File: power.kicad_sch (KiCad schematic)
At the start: 4 parts, among them J1 USB_C_Receptacle_USB2.0_14P, U3 BQ51051BRHL

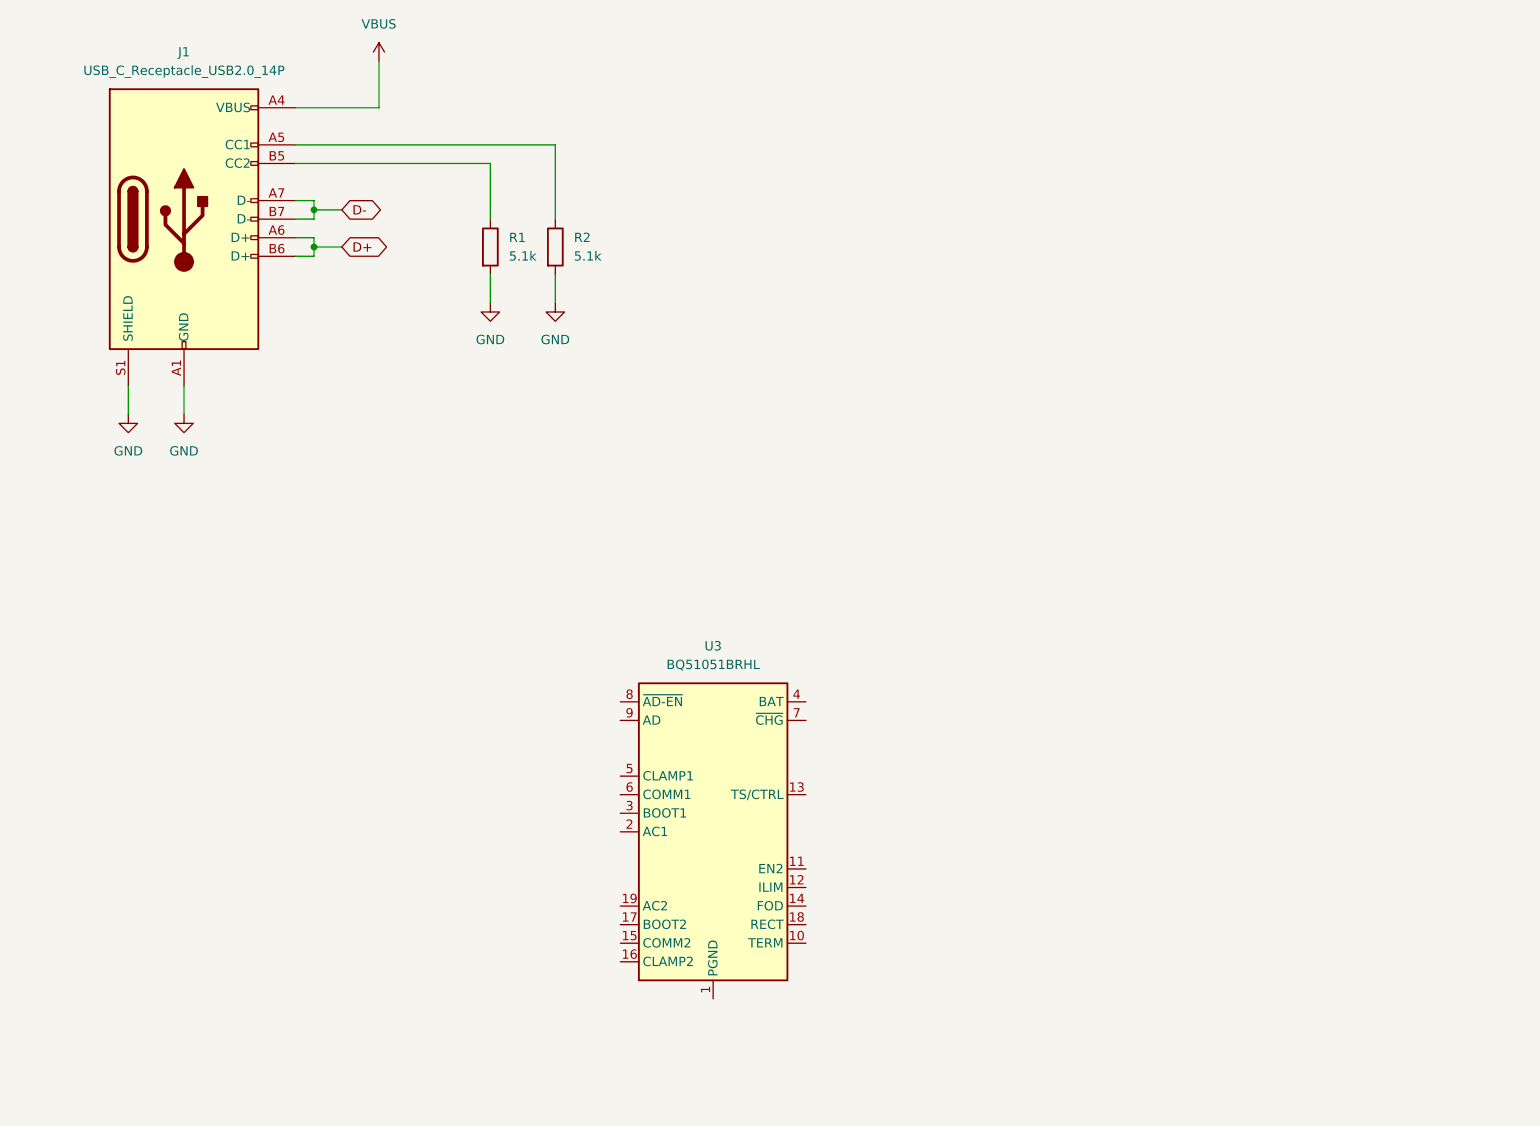
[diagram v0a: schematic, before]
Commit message: Add power rail
Battery charger
3.3V LDO
1.8V LDO
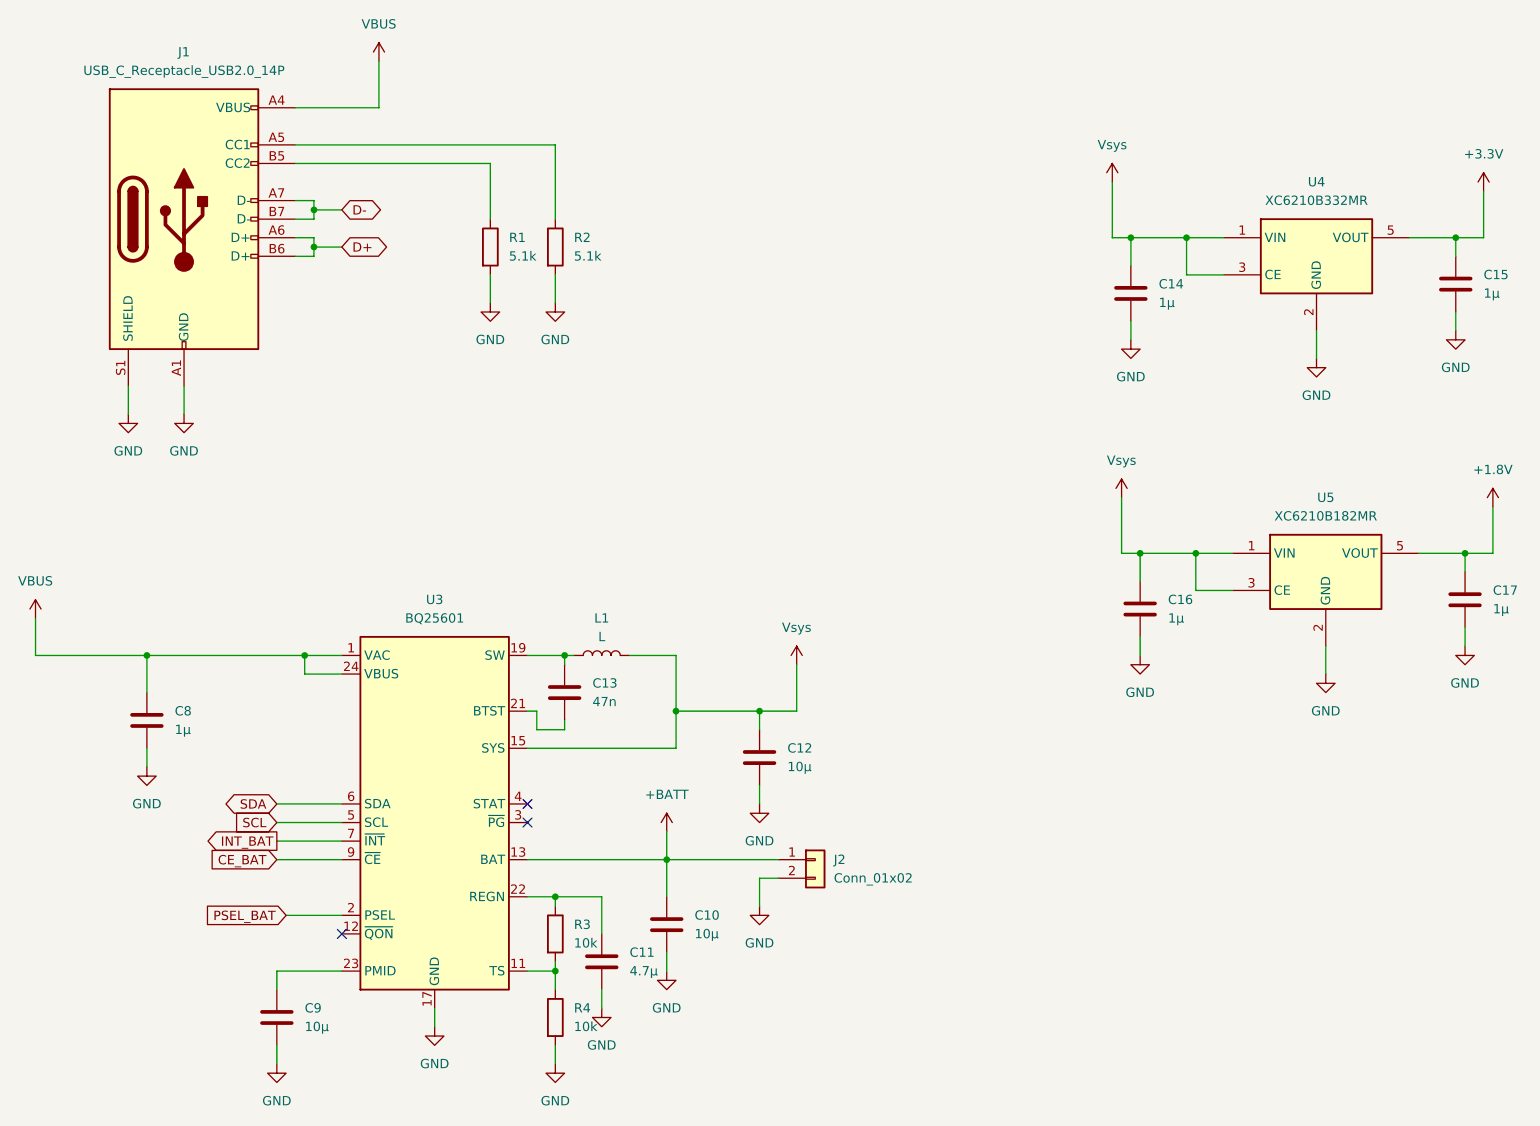
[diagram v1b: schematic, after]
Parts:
- removed U3: BQ51051BRHL, Package_DFN_QFN:Texas_VQFN-RHL-20, symbol Battery_Management:BQ51051BRHL
- added C10, C12, C9: 10µ, symbol Device:C
- added C11: 4.7µ, symbol Device:C
- added C13: 47n, symbol Device:C
- added C14, C15, C16, C17, C8: 1µ, symbol Device:C
- added J2: Conn_01x02, symbol Connector_Generic:Conn_01x02
- added L1: L, symbol Device:L
- added R3, R4: 10k, symbol Device:R
- added U3: BQ25601, Package_DFN_QFN:Texas_RTW_WQFN-24-1EP_4x4mm_P0.5mm_EP2.7x2.7mm_ThermalVias, symbol Battery_Management:BQ25601
- added U4: XC6210B332MR, Package_TO_SOT_SMD:SOT-23-5, symbol Regulator_Linear:XC6210B332MR
- added U5: XC6210B182MR, Package_TO_SOT_SMD:SOT-23-5, symbol Regulator_Linear:XC6210B332MR
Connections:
- net GND: now also C10.2, C11.2, C12.2, C14.2, C15.2, C16.2, C17.2, C8.2, C9.2, J2.2 (Pin_2), R4.2, U3.17 (GND), U3.18 (GND), U3.25 (GND), U4.2 (GND), U5.2 (GND)
- net VBUS: now also C8.1, U3.1 (VAC), U3.24 (VBUS)
- new net: C11.1, R3.1, U3.22 (REGN)
- new net: R3.2, R4.1, U3.11 (TS)
- new net: C13.1, L1.1, U3.19 (SW), U3.20 (SW)
- new net: C13.2, U3.21 (BTST)
- new net: C9.1, U3.23 (PMID)
- new net +1.8V: C17.1, U5.5 (VOUT)
- new net +3.3V: C15.1, U4.5 (VOUT)
- new net +BATT: C10.1, J2.1 (Pin_1), U3.13 (BAT), U3.14 (BAT)
- new net CE_BAT: U3.9 (~{CE})
- new net INT_BAT: U3.7 (~{INT})
- new net PSEL_BAT: U3.2 (PSEL)
- new net SCL: U3.5 (SCL)
- new net SDA: U3.6 (SDA)
- new net Vsys: C12.1, C14.1, C16.1, L1.2, U3.15 (SYS), U3.16 (SYS), U4.1 (VIN), U4.3 (CE), U5.1 (VIN), U5.3 (CE)
- no-connect marks 0 -> 3

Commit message: Routage complet
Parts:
- C10, C11, C12, C13, C14, C15, C16, C17, C8, C9: footprint (none) -> Capacitor_SMD:C_0805_2012Metric
- J1: value USB_C_Receptacle_USB2.0_14P -> USB4105-GF-A-120; footprint (none) -> Connector_USB:USB_C_Receptacle_GCT_USB4105-xx-A_16P_TopMnt_Horizontal
- J2: value Conn_01x02 -> S2B-PH-SM4-TB; footprint (none) -> Connector_JST:JST_PH_S2B-PH-SM4-TB_1x02-1MP_P2.00mm_Horizontal
- L1: value L -> 1µ; footprint (none) -> Inductor_SMD:L_2010_5025Metric
- R1, R2, R3, R4: footprint (none) -> Resistor_SMD:R_0805_2012Metric
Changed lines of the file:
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@@
 			)
 		)
-		(property "Footprint" ""
+		(property "Footprint" "Capacitor_SMD:C_0805_2012Metric"
 			(at 133.0452 125.73 0)
 			(effects
@@
 			)
 		)
-		(property "Footprint" ""
+		(property "Footprint" "Resistor_SMD:R_0805_2012Metric"
 			(at 93.472 52.07 90)
 			(effects
@@
 			)
 		)
-		(property "Footprint" ""
+		(property "Footprint" "Capacitor_SMD:C_0805_2012Metric"
 			(at 183.8452 62.23 0)
 			(effects
@@
 			)
 		)
-		(property "Footprint" ""
+		(property "Footprint" "Capacitor_SMD:C_0805_2012Metric"
 			(at 120.3452 148.59 0)
 			(effects
@@
 			)
 		)
-		(property "Footprint" ""
+		(property "Footprint" "Resistor_SMD:R_0805_2012Metric"
 			(at 102.362 146.05 90)
 			(effects
@@
 			)
 		)
-		(property "Footprint" ""
+		(property "Footprint" "Capacitor_SMD:C_0805_2012Metric"
 			(at 229.5652 104.14 0)
 			(effects
@@
 			)
 		)
-		(property "Footprint" ""
+		(property "Footprint" "Capacitor_SMD:C_0805_2012Metric"
 			(at 111.4552 153.67 0)
 			(effects
@@
 			)
 		)
-		(property "Footprint" ""
+		(property "Footprint" "Resistor_SMD:R_0805_2012Metric"
 			(at 102.362 52.07 90)
 			(effects
@@
 			)
 		)
-		(property "Footprint" ""
+		(property "Footprint" "Capacitor_SMD:C_0805_2012Metric"
 			(at 106.3752 116.84 0)
 			(effects
@@
 			)
 		)
-		(property "Value" "L"
+		(property "Value" "1µ"
 			(at 110.49 105.41 90)
 			(effects
@@
 			)
 		)
-		(property "Footprint" ""
+		(property "Footprint" "Inductor_SMD:L_2010_5025Metric"
 			(at 110.49 107.95 0)
 			(effects
@@
 			)
 		)
-		(property "Footprint" ""
+		(property "Footprint" "Capacitor_SMD:C_0805_2012Metric"
 			(at 185.1152 105.41 0)
 			(effects
@@
 			)
 		)
-		(property "Footprint" ""
+		(property "Footprint" "Capacitor_SMD:C_0805_2012Metric"
 			(at 49.2252 120.65 0)
 			(effects
@@
 			)
 		)
-		(property "Value" "Conn_01x02"
+		(property "Value" "S2B-PH-SM4-TB"
 			(at 142.24 138.4299 0)
 			(effects
@@
 			)
 		)
-		(property "Footprint" ""
+		(property "Footprint" "Connector_JST:JST_PH_S2B-PH-SM4-TB_1x02-1MP_P2.00mm_Horizontal"
 			(at 139.7 135.89 0)
 			(effects
@@
 			)
 		)
-		(property "Footprint" ""
+		(property "Footprint" "Capacitor_SMD:C_0805_2012Metric"
 			(at 228.2952 60.96 0)
 			(effects
@@
 			)
 		)
-		(property "Value" "USB_C_Receptacle_USB2.0_14P"
+		(property "Value" "USB4105-GF-A-120"
 			(at 53.34 27.94 0)
 			(effects
@@
 			)
 		)
-		(property "Footprint" ""
+		(property "Footprint" "Connector_USB:USB_C_Receptacle_GCT_USB4105-xx-A_16P_TopMnt_Horizontal"
 			(at 57.15 48.26 0)
 			(effects
@@
 			)
 		)
-		(property "Footprint" ""
+		(property "Footprint" "Resistor_SMD:R_0805_2012Metric"
 			(at 102.362 157.48 90)
 			(effects
@@
 			)
 		)
-		(property "Footprint" ""
+		(property "Footprint" "Capacitor_SMD:C_0805_2012Metric"
 			(at 67.0052 161.29 0)
 			(effects

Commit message: Set MPN
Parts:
- C10, C12, C9: JLCPCB Part # (none) -> CL21B106KPQNNNE; manf# (none) -> CL21B106KPQNNNE
- C11: JLCPCB Part # (none) -> C2012X7R1A475KT000N; manf# (none) -> C2012X7R1A475KT000N
- C13: JLCPCB Part # (none) -> 0805B473K500NT; manf# (none) -> 0805B473K500NT
- C14, C15, C16, C17, C8: JLCPCB Part # (none) -> CL21B105KAFNFNE; manf# (none) -> CL21B105KAFNFNE
- J1: JLCPCB Part # (none) -> USB4105-GF-A-120; manf# (none) -> USB4105-GF-A-120
- J2: now not fitted; now left out of the parts list
- L1: footprint Inductor_SMD:L_2010_5025Metric -> Inductor_SMD:L_0805_2012Metric; JLCPCB Part # (none) -> LQM21PH1R0NGCD; manf# (none) -> LQM21PH1R0NGCD
- R1, R2: JLCPCB Part # (none) -> RK73H2ATTD5101F; manf# (none) -> RK73H2ATTD5101F
- R3, R4: JLCPCB Part # (none) -> RK73H2ATTD1002F; manf# (none) -> RK73H2ATTD1002F
- U3: JLCPCB Part # (none) -> BQ25601DRTWR; manf# (none) -> BQ25601DRTWR
- U4: JLCPCB Part # (none) -> XC6210B332MR; manf# (none) -> XC6210B332MR
- U5: JLCPCB Part # (none) -> XC6210B182MR; manf# (none) -> XC6210B182MR

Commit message: Change Code for JLC part
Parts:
- C10, C12, C9: JLCPCB Part # CL21B106KPQNNNE -> C32635
- C11: JLCPCB Part # C2012X7R1A475KT000N -> C76639
- C13: JLCPCB Part # 0805B473K500NT -> C1745
- C14, C15, C16, C17, C8: JLCPCB Part # CL21B105KAFNFNE -> C1712
- J1: JLCPCB Part # USB4105-GF-A-120 -> C5184243
- L1: JLCPCB Part # LQM21PH1R0NGCD -> C484262
- R1, R2: JLCPCB Part # RK73H2ATTD5101F -> C317272
- R3, R4: JLCPCB Part # RK73H2ATTD1002F -> C276215
- U3: JLCPCB Part # BQ25601DRTWR -> C2859691
- U4: JLCPCB Part # XC6210B332MR -> C424705
- U5: JLCPCB Part # XC6210B182MR -> C2983925
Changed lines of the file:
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@@
 			)
 		)
-		(property "JLCPCB Part #" "XC6210B182MR"
+		(property "JLCPCB Part #" "C2983925"
 			(at 209.55 96.52 0)
 			(effects
@@
 			)
 		)
-		(property "JLCPCB Part #" "CL21B106KPQNNNE"
+		(property "JLCPCB Part #" "C32635"
 			(at 132.08 121.92 0)
 			(effects
@@
 			)
 		)
-		(property "JLCPCB Part #" "RK73H2ATTD5101F"
+		(property "JLCPCB Part #" "C317272"
 			(at 95.25 52.07 0)
 			(effects
@@
 			)
 		)
-		(property "JLCPCB Part #" "CL21B105KAFNFNE"
+		(property "JLCPCB Part #" "C1712"
 			(at 182.88 58.42 0)
 			(effects
@@
 			)
 		)
-		(property "JLCPCB Part #" "CL21B106KPQNNNE"
+		(property "JLCPCB Part #" "C32635"
 			(at 119.38 144.78 0)
 			(effects
@@
 			)
 		)
-		(property "JLCPCB Part #" "RK73H2ATTD1002F"
+		(property "JLCPCB Part #" "C276215"
 			(at 104.14 146.05 0)
 			(effects
@@
 			)
 		)
-		(property "JLCPCB Part #" "BQ25601DRTWR"
+		(property "JLCPCB Part #" "C2859691"
 			(at 87.63 130.81 0)
 			(effects
@@
 			)
 		)
-		(property "JLCPCB Part #" "CL21B105KAFNFNE"
+		(property "JLCPCB Part #" "C1712"
 			(at 228.6 100.33 0)
 			(effects
@@
 			)
 		)
-		(property "JLCPCB Part #" "C2012X7R1A475KT000N"
+		(property "JLCPCB Part #" "C76639"
 			(at 110.49 149.86 0)
 			(effects
@@
 			)
 		)
-		(property "JLCPCB Part #" "RK73H2ATTD5101F"
+		(property "JLCPCB Part #" "C317272"
 			(at 104.14 52.07 0)
 			(effects
@@
 			)
 		)
-		(property "JLCPCB Part #" "0805B473K500NT"
+		(property "JLCPCB Part #" "C1745"
 			(at 105.41 113.03 0)
 			(effects
@@
 			)
 		)
-		(property "JLCPCB Part #" "LQM21PH1R0NGCD"
+		(property "JLCPCB Part #" "C484262"
 			(at 110.49 107.95 90)
 			(effects
@@
 			)
 		)
-		(property "JLCPCB Part #" "CL21B105KAFNFNE"
+		(property "JLCPCB Part #" "C1712"
 			(at 184.15 101.6 0)
 			(effects
@@
 			)
 		)
-		(property "JLCPCB Part #" "XC6210B332MR"
+		(property "JLCPCB Part #" "C424705"
 			(at 208.28 53.34 0)
 			(effects
@@
 			)
 		)
-		(property "JLCPCB Part #" "CL21B105KAFNFNE"
+		(property "JLCPCB Part #" "C1712"
 			(at 48.26 116.84 0)
 			(effects
@@
 			)
 		)
-		(property "JLCPCB Part #" "CL21B105KAFNFNE"
+		(property "JLCPCB Part #" "C1712"
 			(at 227.33 57.15 0)
 			(effects
@@
 			)
 		)
-		(property "JLCPCB Part #" "USB4105-GF-A-120"
+		(property "JLCPCB Part #" "C5184243"
 			(at 53.34 48.26 0)
 			(effects
@@
 			)
 		)
-		(property "JLCPCB Part #" "RK73H2ATTD1002F"
+		(property "JLCPCB Part #" "C276215"
 			(at 104.14 157.48 0)
 			(effects
@@
 			)
 		)
-		(property "JLCPCB Part #" "CL21B106KPQNNNE"
+		(property "JLCPCB Part #" "C32635"
 			(at 66.04 157.48 0)
 			(effects

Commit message: Add version
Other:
- company: (none) -> Philippe12
- title: (none) -> HorseSense
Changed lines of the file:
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@@
 	(generator_version "9.0")
 	(paper "A4")
+	(title_block
+		(title "HorseSense")
+		(date "2025-11-01")
+		(rev "1.0")
+		(company "Philippe12")
+	)
 	(junction
 		(at 182.88 50.8)

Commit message: Update for JLC parts
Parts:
- J1: value USB4105-GF-A-120 -> 1054500101; JLCPCB Part # C5184243 -> C134092; manf# USB4105-GF-A-120 -> 1054500101
- L1: JLCPCB Part # C484262 -> C383371; manf# LQM21PH1R0NGCD -> MLP2012S1R0MT0S1
- R1, R2: JLCPCB Part # C317272 -> C27834; manf# RK73H2ATTD5101F -> 0805W8F5101T5E
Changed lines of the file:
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@@
 			)
 		)
-		(property "Sim.Enable" ""
+		(property "SnapEDA_Link" ""
 			(at 209.55 96.52 0)
 			(effects
@@
 			)
 		)
-		(property "SnapEDA_Link" ""
+		(property "Sim.Enable" ""
 			(at 209.55 96.52 0)
 			(effects
@@
 			)
 		)
-		(property "Sim.Enable" ""
+		(property "SnapEDA_Link" ""
 			(at 132.08 121.92 0)
 			(effects
@@
 			)
 		)
-		(property "SnapEDA_Link" ""
+		(property "Sim.Enable" ""
 			(at 132.08 121.92 0)
 			(effects
@@
 			)
 		)
-		(property "JLCPCB Part #" "C317272"
+		(property "JLCPCB Part #" "C27834"
 			(at 95.25 52.07 0)
 			(effects
@@
 			)
 		)
-		(property "manf#" "RK73H2ATTD5101F"
+		(property "manf#" "0805W8F5101T5E"
 			(at 95.25 52.07 0)
 			(effects
@@
 			)
 		)
-		(property "Sim.Enable" ""
+		(property "SnapEDA_Link" ""
 			(at 95.25 52.07 0)
 			(effects
@@
 			)
 		)
-		(property "SnapEDA_Link" ""
+		(property "Sim.Enable" ""
 			(at 95.25 52.07 0)
 			(effects
@@
 			)
 		)
-		(property "Sim.Enable" ""
+		(property "SnapEDA_Link" ""
 			(at 182.88 58.42 0)
 			(effects
@@
 			)
 		)
-		(property "SnapEDA_Link" ""
+		(property "Sim.Enable" ""
 			(at 182.88 58.42 0)
 			(effects
@@
 			)
 		)
-		(property "Sim.Enable" ""
+		(property "SnapEDA_Link" ""
 			(at 119.38 144.78 0)
 			(effects
@@
 			)
 		)
-		(property "SnapEDA_Link" ""
+		(property "Sim.Enable" ""
 			(at 119.38 144.78 0)
 			(effects
@@
 			)
 		)
-		(property "Sim.Enable" ""
+		(property "SnapEDA_Link" ""
 			(at 104.14 146.05 0)
 			(effects
@@
 			)
 		)
-		(property "SnapEDA_Link" ""
+		(property "Sim.Enable" ""
 			(at 104.14 146.05 0)
 			(effects
@@
 			)
 		)
-		(property "Sim.Enable" ""
+		(property "SnapEDA_Link" ""
 			(at 87.63 130.81 0)
 			(effects
@@
 			)
 		)
-		(property "SnapEDA_Link" ""
+		(property "Sim.Enable" ""
 			(at 87.63 130.81 0)
 			(effects
@@
 			)
 		)
-		(property "Sim.Enable" ""
+		(property "SnapEDA_Link" ""
 			(at 228.6 100.33 0)
 			(effects
@@
 			)
 		)
-		(property "SnapEDA_Link" ""
+		(property "Sim.Enable" ""
 			(at 228.6 100.33 0)
 			(effects
@@
 			)
 		)
-		(property "Sim.Enable" ""
+		(property "SnapEDA_Link" ""
 			(at 110.49 149.86 0)
 			(effects
@@
 			)
 		)
-		(property "SnapEDA_Link" ""
+		(property "Sim.Enable" ""
 			(at 110.49 149.86 0)
 			(effects
@@
 			)
 		)
-		(property "JLCPCB Part #" "C317272"
+		(property "JLCPCB Part #" "C27834"
 			(at 104.14 52.07 0)
 			(effects
@@
 			)
 		)
-		(property "manf#" "RK73H2ATTD5101F"
+		(property "manf#" "0805W8F5101T5E"
 			(at 104.14 52.07 0)
 			(effects
@@
 			)
 		)
-		(property "Sim.Enable" ""
+		(property "SnapEDA_Link" ""
 			(at 104.14 52.07 0)
 			(effects
@@
 			)
 		)
-		(property "SnapEDA_Link" ""
+		(property "Sim.Enable" ""
 			(at 104.14 52.07 0)
 			(effects
@@
 			)
 		)
-		(property "Sim.Enable" ""
+		(property "SnapEDA_Link" ""
 			(at 105.41 113.03 0)
 			(effects
@@
 			)
 		)
-		(property "SnapEDA_Link" ""
+		(property "Sim.Enable" ""
 			(at 105.41 113.03 0)
 			(effects
@@
 			)
 		)
-		(property "manf#" "LQM21PH1R0NGCD"
+		(property "manf#" "MLP2012S1R0MT0S1"
 			(at 110.49 107.95 90)
 			(effects
@@
 			)
 		)
-		(property "JLCPCB Part #" "C484262"
+		(property "JLCPCB Part #" "C383371"
 			(at 110.49 107.95 90)
 			(effects
@@
 			)
 		)
-		(property "Sim.Enable" ""
+		(property "SnapEDA_Link" ""
 			(at 110.49 107.95 90)
 			(effects
@@
 			)
 		)
-		(property "SnapEDA_Link" ""
+		(property "Sim.Enable" ""
 			(at 110.49 107.95 90)
 			(effects
@@
 			)
 		)
-		(property "Sim.Enable" ""
+		(property "SnapEDA_Link" ""
 			(at 184.15 101.6 0)
 			(effects
@@
 			)
 		)
-		(property "SnapEDA_Link" ""
+		(property "Sim.Enable" ""
 			(at 184.15 101.6 0)
 			(effects
@@
 			)
 		)
-		(property "Sim.Enable" ""
+		(property "SnapEDA_Link" ""
 			(at 208.28 53.34 0)
 			(effects
@@
 			)
 		)
-		(property "SnapEDA_Link" ""
+		(property "Sim.Enable" ""
 			(at 208.28 53.34 0)
 			(effects
@@
 			)
 		)
-		(property "Sim.Enable" ""
+		(property "SnapEDA_Link" ""
 			(at 48.26 116.84 0)
 			(effects
@@
 			)
 		)
-		(property "SnapEDA_Link" ""
+		(property "Sim.Enable" ""
 			(at 48.26 116.84 0)
 			(effects
@@
 			)
 		)
-		(property "Sim.Enable" ""
+		(property "SnapEDA_Link" ""
 			(at 139.7 135.89 0)
 			(effects
@@
 			)
 		)
-		(property "SnapEDA_Link" ""
+		(property "Sim.Enable" ""
 			(at 139.7 135.89 0)
 			(effects
@@
 			)
 		)
-		(property "Sim.Enable" ""
+		(property "SnapEDA_Link" ""
 			(at 227.33 57.15 0)
 			(effects
@@
 			)
 		)
-		(property "SnapEDA_Link" ""
+		(property "Sim.Enable" ""
 			(at 227.33 57.15 0)
 			(effects
@@
 			)
 		)
-		(property "Value" "USB4105-GF-A-120"
+		(property "Value" "1054500101"
 			(at 53.34 27.94 0)
 			(effects
@@
 			)
 		)
-		(property "manf#" "USB4105-GF-A-120"
+		(property "manf#" "1054500101"
 			(at 53.34 48.26 0)
 			(effects
@@
 			)
 		)
-		(property "JLCPCB Part #" "C5184243"
+		(property "JLCPCB Part #" "C134092"
 			(at 53.34 48.26 0)
 			(effects
@@
 			)
 		)
-		(property "Sim.Enable" ""
+		(property "SnapEDA_Link" ""
 			(at 53.34 48.26 0)
 			(effects
@@
 			)
 		)
-		(property "SnapEDA_Link" ""
+		(property "Sim.Enable" ""
 			(at 53.34 48.26 0)
 			(effects
@@
 			)
 		)
-		(property "Sim.Enable" ""
+		(property "SnapEDA_Link" ""
 			(at 104.14 157.48 0)
 			(effects
@@
 			)
 		)
-		(property "SnapEDA_Link" ""
+		(property "Sim.Enable" ""
 			(at 104.14 157.48 0)
 			(effects
@@
 			)
 		)
-		(property "Sim.Enable" ""
+		(property "SnapEDA_Link" ""
 			(at 66.04 157.48 0)
 			(effects
@@
 			)
 		)
-		(property "SnapEDA_Link" ""
+		(property "Sim.Enable" ""
 			(at 66.04 157.48 0)
 			(effects
